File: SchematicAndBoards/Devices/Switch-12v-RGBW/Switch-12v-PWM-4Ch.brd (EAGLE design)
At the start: 83.2 x 62.1 mm, 66 parts, among them IC1 REG1117, IC2 IR4427S, IC3 IR4427S, Q1 IRF7805, Q2 IRF7805, Q3 IRF7805, Q4 IRF7805

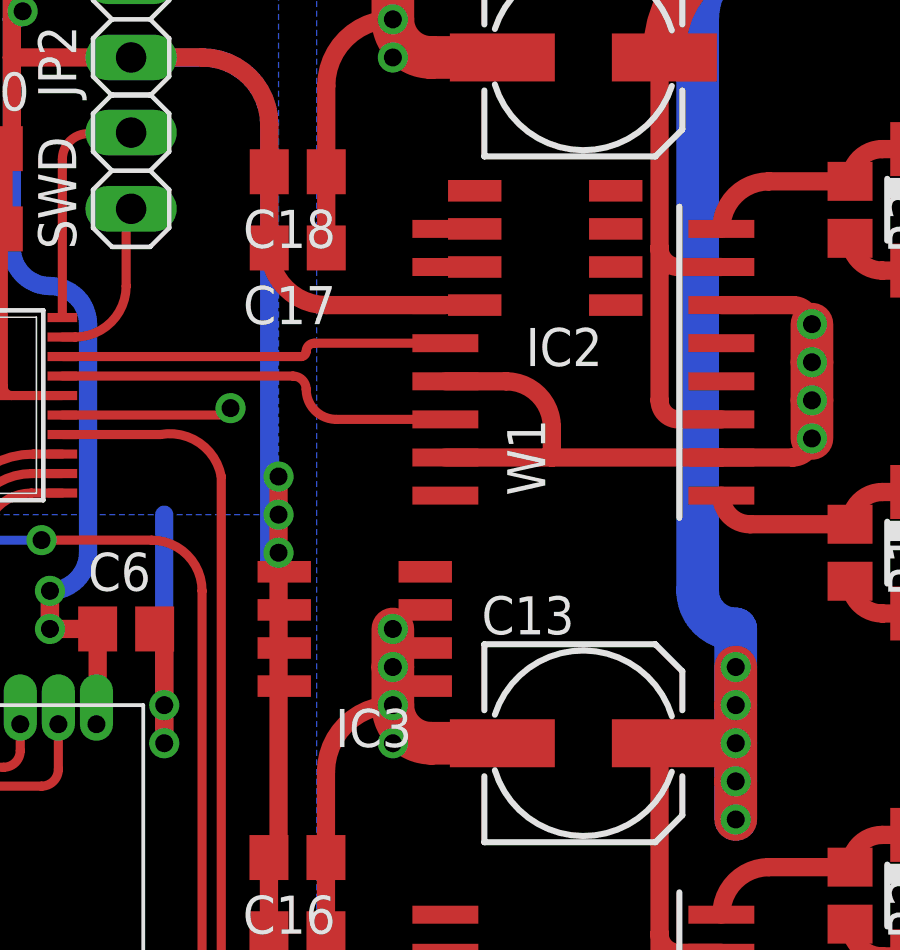
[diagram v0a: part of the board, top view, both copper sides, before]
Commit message: Update Switch-12v-PWM-4Ch
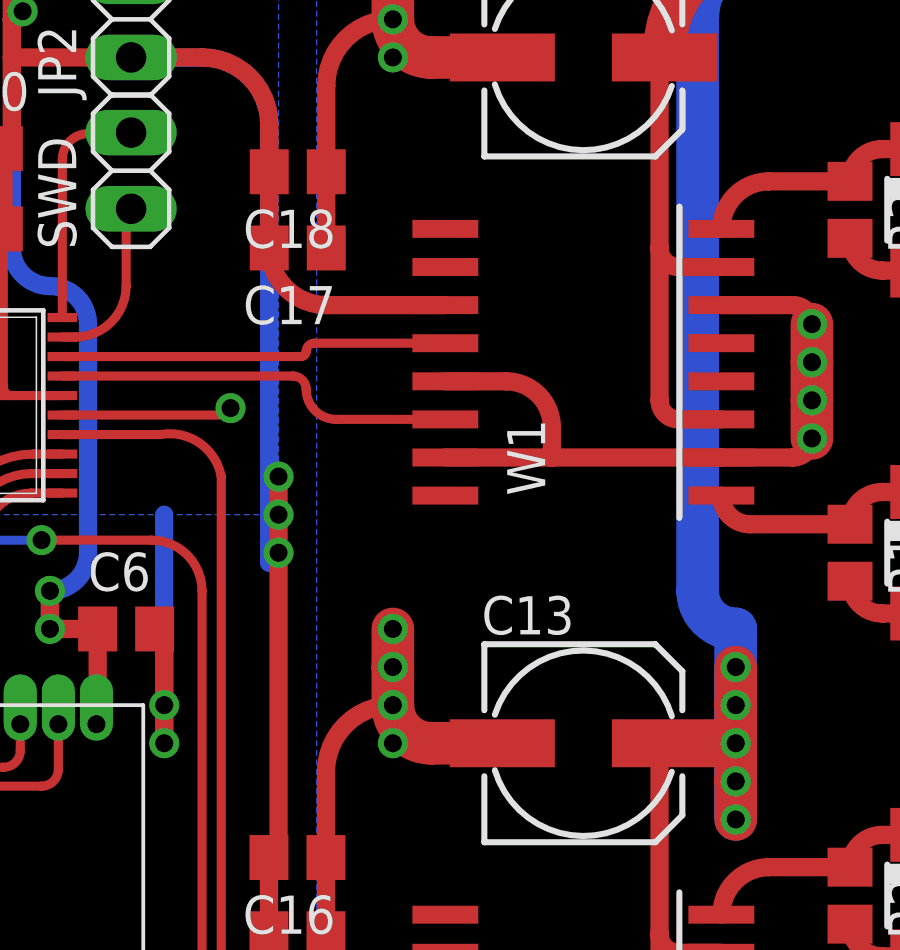
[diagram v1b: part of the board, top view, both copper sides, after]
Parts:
- removed IC2, IC3: IR4427S, ir:SO08
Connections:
- removed net VS: IC3.6
- net GND: no longer IC2.3, IC3.3
- net IN12V: no longer IC2.6
- net PWM-CH1-I: no longer IC2.7
- net PWM-CH2-I: no longer IC2.5
- net PWM_1: no longer IC2.2
- net PWM_2: no longer IC2.4
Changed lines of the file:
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@@
 <element name="JP2" library="pinhead" package="1X02" value="" x="14.135" y="45.72" rot="R90"/>
 <element name="JP3" library="pinhead" package="1X01" value="" x="3.18" y="34.29"/>
-<element name="IC2" library="ir" package="SO08" value="IR4427S" x="27.94" y="38.1" rot="R90">
-<attribute name="OC_NEWARK" value="63J7933" x="27.94" y="38.1" size="1.778" layer="27" rot="R90" display="off"/>
-<attribute name="MPN" value="IR4427STRPBF" x="27.94" y="38.1" size="1.778" layer="27" rot="R90" display="off"/>
-<attribute name="MF" value="INTERNATIONAL RECTIFIER(IR)" x="27.94" y="38.1" size="1.778" layer="27" rot="R90" display="off"/>
-<attribute name="OC_FARNELL" value="8639094" x="27.94" y="38.1" size="1.778" layer="27" rot="R90" display="off"/>
-</element>
-<element name="IC3" library="ir" package="SO08" value="IR4427S" x="21.59" y="25.4" rot="R90">
-<attribute name="OC_NEWARK" value="63J7933" x="21.59" y="25.4" size="1.778" layer="27" rot="R90" display="off"/>
-<attribute name="MPN" value="IR4427STRPBF" x="21.59" y="25.4" size="1.778" layer="27" rot="R90" display="off"/>
-<attribute name="MF" value="INTERNATIONAL RECTIFIER(IR)" x="21.59" y="25.4" size="1.778" layer="27" rot="R90" display="off"/>
-<attribute name="OC_FARNELL" value="8639094" x="21.59" y="25.4" size="1.778" layer="27" rot="R90" display="off"/>
-</element>
 </elements>
 <signals>
@@
 <wire x1="3.175" y1="22.225" x2="2.54" y2="22.86" width="0.6096" layer="16" curve="-90"/>
 <wire x1="2.54" y1="22.86" x2="2.54" y2="29.21" width="0.6096" layer="16"/>
-<contactref element="IC3" pad="3"/>
-<contactref element="IC2" pad="3"/>
-<wire x1="28.16" y1="31.115" x2="23.94" y2="26.035" width="0" layer="19" extent="1-1"/>
-<wire x1="30.29" y1="38.735" x2="33.81" y2="8.255" width="0" layer="19" extent="1-1"/>
 </signal>
 <signal name="CE">
@@
 <vertex x="73.66" y="1.27"/>
 </polygon>
-<contactref element="IC2" pad="6"/>
-<wire x1="32.385" y1="9.525" x2="25.59" y2="38.735" width="0" layer="19" extent="1-1"/>
 </signal>
 <signal name="PWM_1">
@@
 <wire x1="19.97" y1="34.65" x2="20.245" y2="34.925" width="0.3048" layer="1" curve="-90"/>
 <wire x1="20.245" y1="34.925" x2="24.61" y2="34.925" width="0.3048" layer="1"/>
-<contactref element="IC2" pad="2"/>
-<wire x1="30.29" y1="37.465" x2="24.61" y2="34.925" width="0" layer="19" extent="1-1"/>
 </signal>
 <signal name="PWM_3">
@@
 <wire x1="24.61" y1="32.385" x2="20.975" y2="32.385" width="0.3048" layer="1"/>
 <wire x1="20.975" y1="32.385" x2="19.97" y2="33.39" width="0.3048" layer="1" curve="-90"/>
-<contactref element="IC2" pad="4"/>
-<wire x1="30.29" y1="40.005" x2="24.61" y2="32.385" width="0" layer="19" extent="1-1"/>
 </signal>
 <signal name="VDD5">
@@
 <wire x1="33.81" y1="38.735" x2="35.395" y2="40.32" width="0.6096" layer="1" curve="-90"/>
 <wire x1="35.395" y1="40.32" x2="38.1" y2="40.32" width="0.6096" layer="1"/>
-<contactref element="IC2" pad="7"/>
-<wire x1="25.59" y1="37.465" x2="33.81" y2="38.735" width="0" layer="19" extent="1-1"/>
 </signal>
 <signal name="PWM-CH3-I">
@@
 <wire x1="33.81" y1="29.845" x2="34.765" y2="28.89" width="0.6096" layer="1" curve="90"/>
 <wire x1="34.765" y1="28.89" x2="38.1" y2="28.89" width="0.6096" layer="1"/>
-<contactref element="IC2" pad="5"/>
-<wire x1="25.59" y1="40.005" x2="34.765" y2="28.89" width="0" layer="19" extent="1-1"/>
 </signal>
 <signal name="N$1">
@@
 <wire x1="50.8" y1="6.35" x2="50.8" y2="5.08" width="0" layer="19" extent="1-1"/>
 </signal>
-<signal name="VS">
-<contactref element="IC3" pad="6"/>
-</signal>
 </signals>

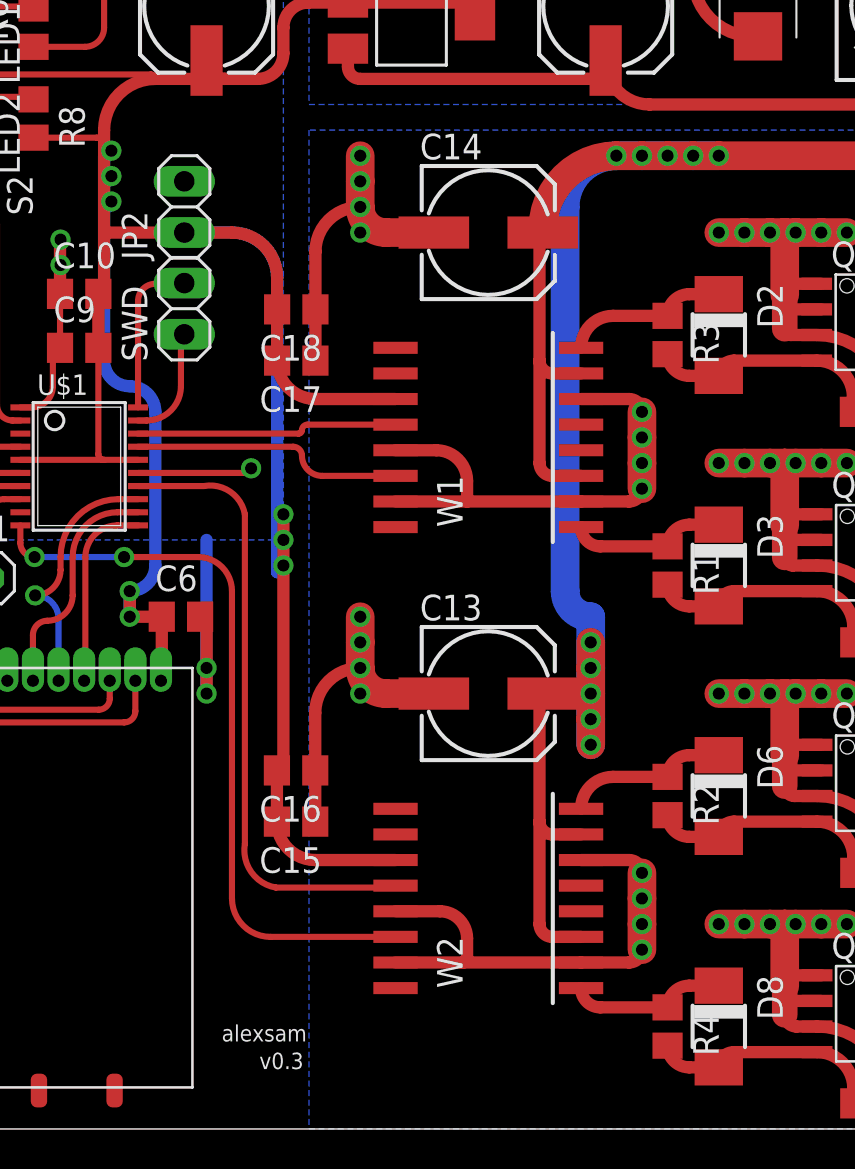
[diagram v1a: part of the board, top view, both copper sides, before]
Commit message: Update Switch-12v-PWM-4Ch - replace driver to IR4427S
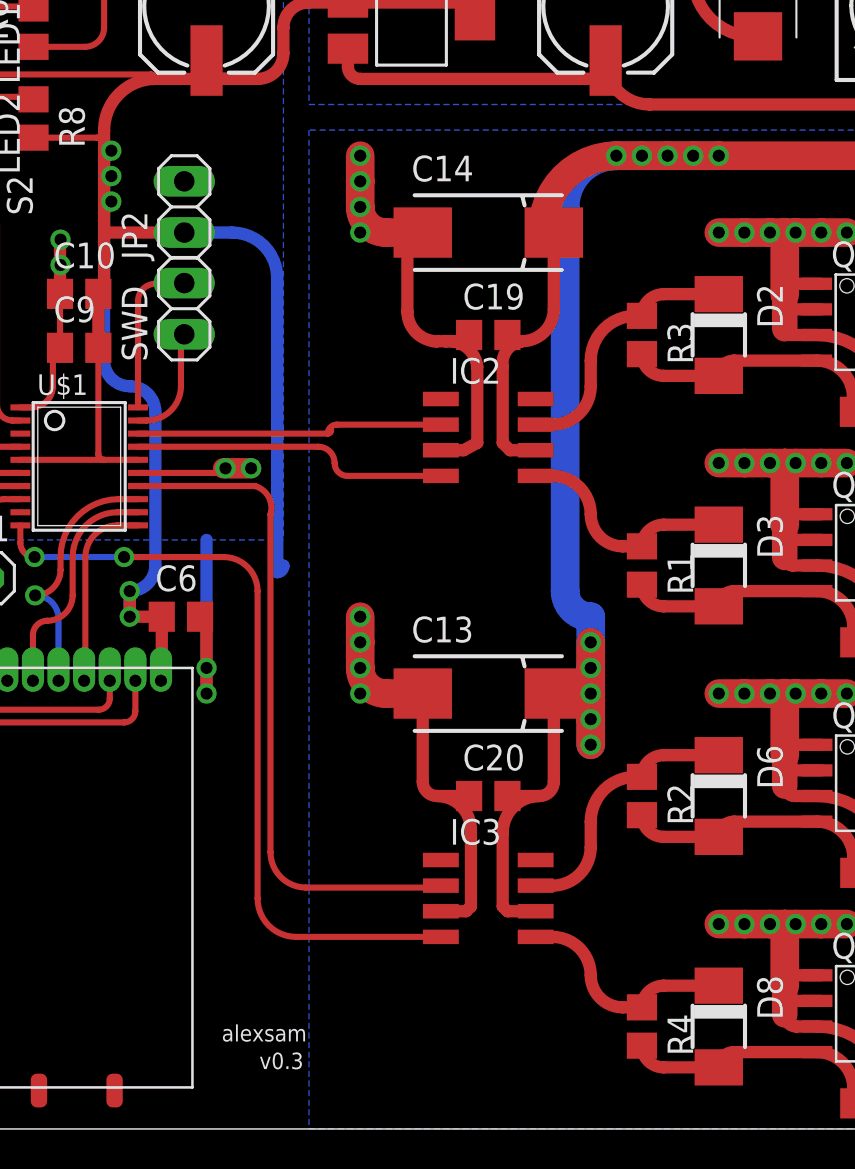
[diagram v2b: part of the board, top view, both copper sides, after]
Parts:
- removed C15, C17: 100 nF, resistor:C0805
- removed C16, C18: 4.7 uF, resistor:C0805
- removed W1: IR2110s, my_components:SO16DW
- removed W2: (no value), my_components:SO16DW
- added C19, C20: 4.7 uF, resistor:C0805
- added IC2, IC3: IR4427S, ir:SO08
- C13, C14: device resistor:153CLV-0605 -> resistor:085CS_1AR
- moved R1 1.27 mm to (36.8, 27.9)
- moved R2 1.27 mm to (36.8, 16.5)
- moved R3 1.27 mm to (36.8, 39.4)
- moved R4 1.27 mm to (36.8, 5.08)
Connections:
- net GND: now also C19.1, C20.1, IC2.3, IC3.3; no longer C15.1, C16.1, C17.1, C18.1, W1.13, W1.15, W1.2, W1.6, W2.13, W2.15, W2.2, W2.6
- net IN12V: now also C19.2, C20.2, IC2.6, IC3.6; no longer W1.3, W1.7, W2.3, W2.7
- net PWM-CH1-I: now also IC2.7; no longer W1.8
- net PWM-CH2-I: now also IC2.5; no longer W1.1
- net PWM-CH3-I: now also IC3.7; no longer W2.8
- net PWM-CH4-I: now also IC3.5; no longer W2.1
- net PWM_1: now also IC2.2; no longer W1.12
- net PWM_2: now also IC2.4; no longer W1.14
- net PWM_3: now also IC3.2; no longer W2.12
- net PWM_4: now also IC3.4; no longer W2.14
- net VDD: no longer C15.2, C16.2, C17.2, C18.2, W1.11, W2.11
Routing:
- net VDD: track 154.6 -> 116.3 mm, vias 8 -> 5
- net GND: track 290.6 -> 254.0 mm, vias 58 -> 51
- net PWM-CH1-I: track 7.93 -> 12.5 mm
- net PWM-CH3-I: track 7.93 -> 12.5 mm
- net IN12V: track 231.0 -> 227.6 mm
- net PWM-CH2-I: track 7.67 -> 11.0 mm
- net PWM-CH4-I: track 7.67 -> 11.0 mm
- net PWM_3: track 30.7 -> 33.4 mm
- net PWM_1: track 13.0 -> 15.4 mm
- net PWM_4: track 36.5 -> 38.7 mm
- net PWM_2: track 13.4 -> 15.6 mm
- net N$5: track 11.5 -> 12.7 mm
- net N$4: track 11.4 -> 12.7 mm
- net N$29: track 11.5 -> 12.7 mm
- net N$26: track 11.5 -> 12.7 mm

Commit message: Update schematic and boards
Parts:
- C11, C12, C7, C8: device resistor:153CLV-0807 -> resistor:E5-8,5
- C2, C3, C5: device resistor:153CLV-0605 -> resistor:SMC_C
- D4, D5, D7, D9: device diode:DO-214AC -> diode:D-7.5
- L2, L3, L4, L5: value DR74 -> 82114R; device inductors:DR74 -> inductors:82114R
- moved D9 4.77 mm to (61.9, 11.4)
- moved D7 4.73 mm to (61.9, 22.2)
- moved D4 4.43 mm to (61.6, 45.1)
- moved D5 4.41 mm to (61.6, 33.6)
- moved C5 1.13 mm to (36.1, 56.1), turned to 90 degrees
- moved C7 0.64 mm to (67.3, 40.0), turned to 270 degrees
- moved C11 0.63 mm to (67.3, 17.1), turned to 270 degrees
- moved C8 0.63 mm to (67.3, 28.6), turned to 270 degrees
- moved R7 0.63 mm to (48.3, 24.8)
- moved R9 0.63 mm to (48.3, 13.3)
- moved R10 0.63 mm to (48.3, 1.90)
- moved R5 0.63 mm to (48.2, 36.2)
- moved C2 0.40 mm to (15.2, 56.1), turned to 90 degrees
- moved C3 0.34 mm to (75.0, 55.7), turned to 270 degrees
- turned C12 to 270 degrees
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- renumbered RSC to R20, RSC1 to R21, RSC2 to R22, U$1 to U1, U$2 to U2
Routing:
- net IN12V: track 227.6 -> 271.9 mm
- net PWM-CH1-O: track 19.3 -> 40.7 mm
- net PWM-CH2-O: track 18.7 -> 39.6 mm
- net PWM-CH3-O: track 18.3 -> 38.9 mm
- net PWM-CH4-O: track 18.4 -> 38.8 mm
- net VDD: track 116.3 -> 96.1 mm
- net N$8: track 18.8 -> 27.6 mm
- net N$10: track 18.8 -> 26.1 mm
- net N$1: track 18.8 -> 26.1 mm
- net N$2: track 18.8 -> 26.0 mm
- net GND: track 254.0 -> 255.6 mm
- net VDD5: track 40.6 -> 41.7 mm
- net N$5: track 12.7 -> 12.1 mm
- net N$29: track 12.7 -> 12.1 mm
- net N$26: track 12.7 -> 12.1 mm
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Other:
- board text added: "GND"
- board text added: "SWCLK"
- board text added: "SWDIO"
- board text added: "USART"
- board text added: "VDD3.3"
- board text added: "alexsam@saewave.com"
- board text added: "nRST"
- board text added: "ver 0.3"
- board text removed: "alexsam"
- board text removed: "v0.3"

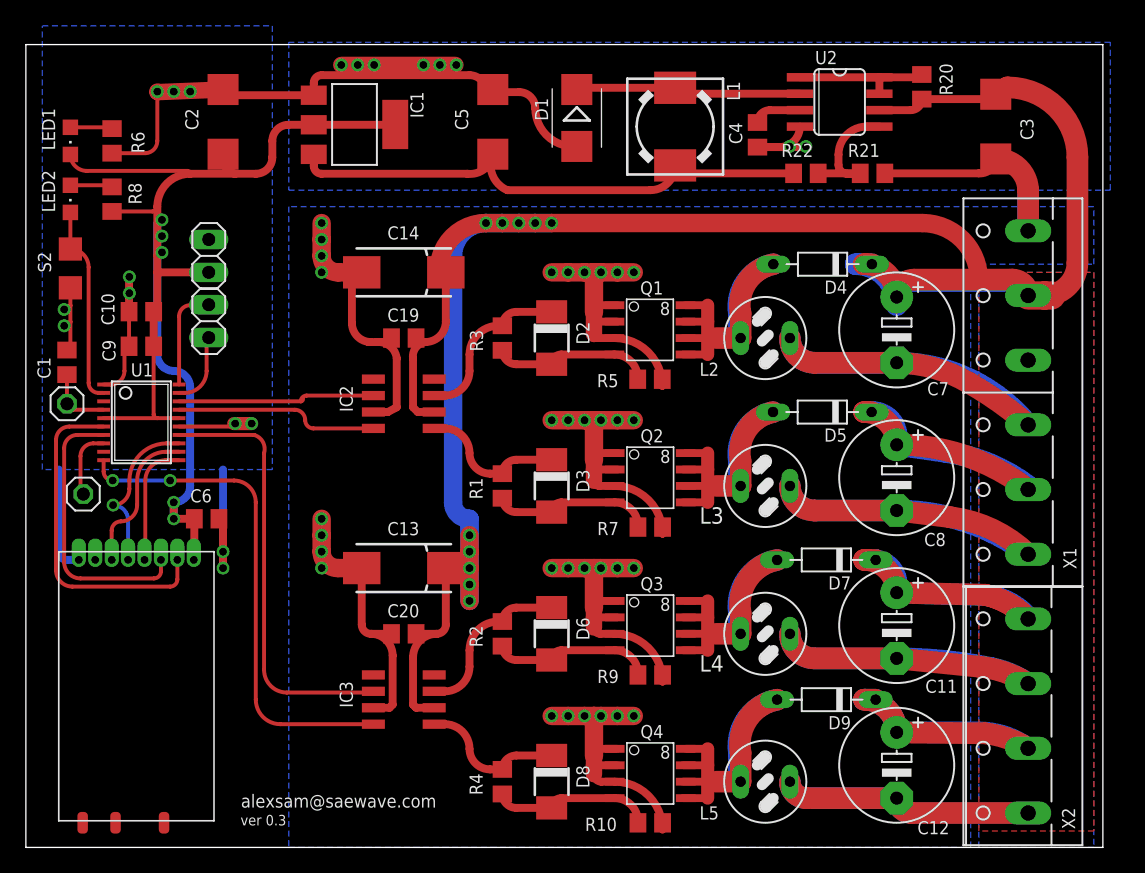
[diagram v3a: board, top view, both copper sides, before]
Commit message: Update Switch-12v-PWM-4Ch schematic
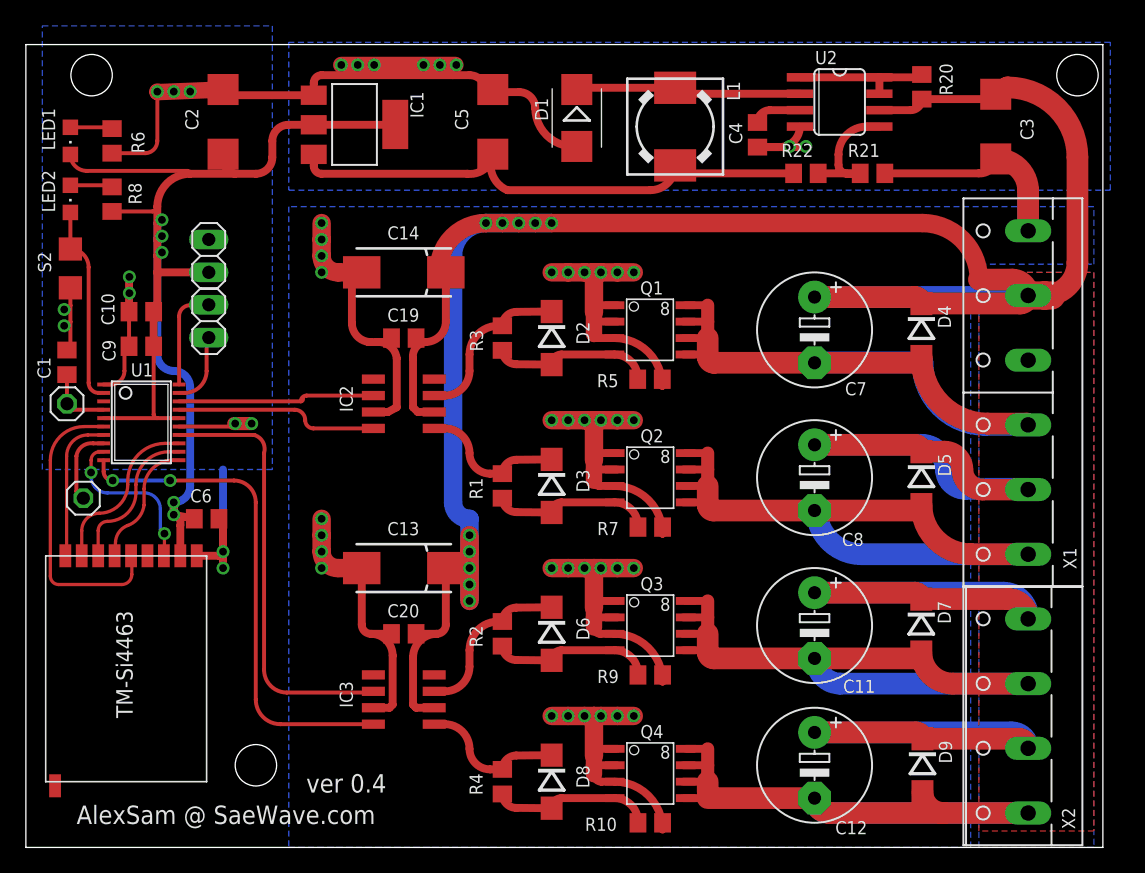
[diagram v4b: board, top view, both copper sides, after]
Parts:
- removed L2, L3, L4, L5: 82114R, inductors:82114R
- removed U$3: AS07-M1101S, RemoteSwitchComponents:AS07-M1101S
- added U$1: TM-SI4463, RemoteSwitchComponents:TM-SI4463-SMD
- D2, D3, D6, D8: device diode:DO-214AC -> diode:DO214BA
- D4, D5, D7, D9: device diode:D-7.5 -> diode:DO214BA
- moved D5 9.21 mm to (69.2, 28.5), turned to 270 degrees
- moved D4 9.18 mm to (69.2, 40.0), turned to 270 degrees
- moved D9 8.99 mm to (69.3, 6.35), turned to 270 degrees
- moved D7 8.92 mm to (69.2, 17.1), turned to 270 degrees
- moved C11 6.35 mm to (61.0, 17.1)
- moved C12 6.35 mm to (61.0, 6.35)
- moved C7 6.35 mm to (61.0, 40.0)
- moved C8 6.35 mm to (61.0, 28.6)
- moved JP1 0.31 mm to (4.44, 27.0)
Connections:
- removed net CE: U1.9
- removed net N$1: D4.A, L2.1, Q1.8
- removed net N$10: D7.A, L4.1, Q3.8
- removed net N$2: D5.A, L3.1, Q2.8
- removed net N$8: D9.A, L5.1, Q4.8
- new net GPIO0: U$1.3, U1.9
- new net N$15: U$1.4
- net CSN: now also U$1.9; no longer U$3.3
- net GND: now also U$1.1; no longer U$3.8
- net IRQ: now also U$1.5; no longer U$3.2
- net MISO: now also U$1.7; no longer U$3.6
- net MOSI: now also U$1.8; no longer U$3.5
- net PWM-CH1-O: now also D4.A, Q1.8; no longer L2.2
- net PWM-CH2-O: now also D5.A, Q2.8; no longer L3.2
- net PWM-CH3-O: now also D7.A, Q3.8; no longer L4.2
- net PWM-CH4-O: now also D9.A, Q4.8; no longer L5.2
- net SCK: now also U$1.6; no longer U$3.4
- net VDD: now also U$1.2; no longer U$3.1
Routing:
- net N$8: track 27.6 -> 0.00 mm
- net N$10: track 26.1 -> 0.00 mm
- net N$1: track 26.1 -> 0.00 mm
- net N$2: track 26.0 -> 0.00 mm
- net IN12V: track 271.9 -> 291.5 mm
- net PWM-CH4-O: track 38.8 -> 56.5 mm
- net PWM-CH1-O: track 40.7 -> 58.4 mm
- net PWM-CH2-O: track 39.6 -> 57.2 mm
- net PWM-CH3-O: track 38.9 -> 55.9 mm
- net GPIO0: track 0.00 -> 12.6 mm, vias 0 -> 2
- net CSN: track 21.4 -> 11.3 mm
- net GND: track 255.6 -> 249.6 mm
- net IRQ: track 25.8 -> 22.5 mm
- net USART_TX: track 5.22 -> 5.90 mm
- net MOSI: track 12.2 -> 12.4 mm, vias 1 -> 0
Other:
- board text added: "AlexSam @ SaeWave.com"
- board text added: "ver 0.4"
- board text removed: "alexsam@saewave.com"
- board text removed: "ver 0.3"
